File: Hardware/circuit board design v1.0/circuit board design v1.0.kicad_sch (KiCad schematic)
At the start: 0 parts

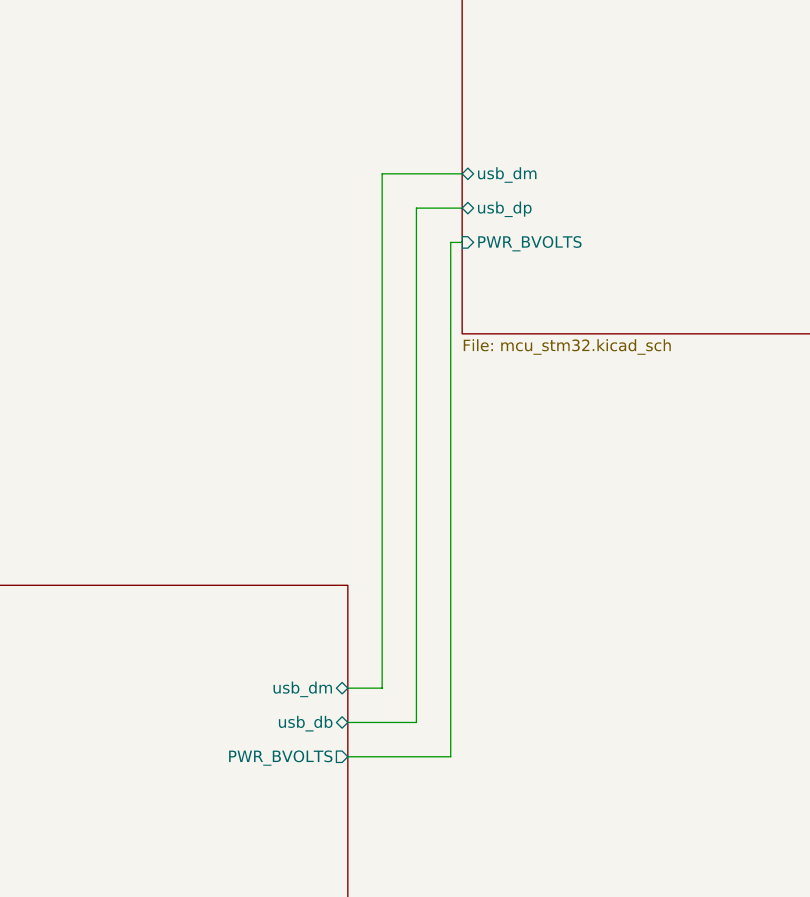
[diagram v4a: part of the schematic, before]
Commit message: Added radio connections to pcb and code
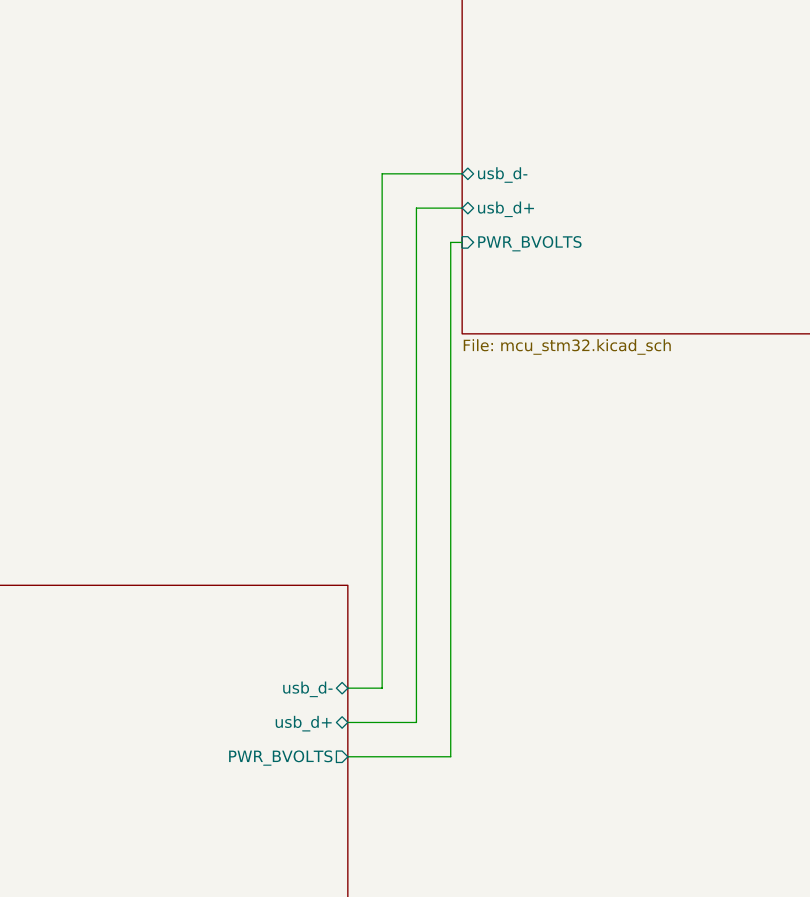
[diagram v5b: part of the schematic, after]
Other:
- sheet MCU ports: added usb_d+, usb_d-; removed usb_dm, usb_dp
- sheet Power ports: added usb_d+, usb_d-; removed usb_db, usb_dm
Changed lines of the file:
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@@
       (effects (font (size 1.27 1.27)) (justify left top))
     )
-    (pin "usb_db" bidirectional (at 78.74 129.54 0)
-      (effects (font (size 1.27 1.27)) (justify right))
-    )
-    (pin "usb_dm" bidirectional (at 78.74 125.73 0)
-      (effects (font (size 1.27 1.27)) (justify right))
-    )
     (pin "PWR_BVOLTS" output (at 78.74 133.35 0)
+      (effects (font (size 1.27 1.27)) (justify right))
+    )
+    (pin "usb_d+" bidirectional (at 78.74 129.54 0)
+      (effects (font (size 1.27 1.27)) (justify right))
+    )
+    (pin "usb_d-" bidirectional (at 78.74 125.73 0)
       (effects (font (size 1.27 1.27)) (justify right))
     )
@@
       (effects (font (size 1.27 1.27)) (justify right))
     )
-    (pin "usb_dp" bidirectional (at 91.44 72.39 180)
+    (pin "UART4_RX" input (at 142.24 67.31 0)
+      (effects (font (size 1.27 1.27)) (justify right))
+    )
+    (pin "UART4_TX" output (at 142.24 71.12 0)
+      (effects (font (size 1.27 1.27)) (justify right))
+    )
+    (pin "PWR_BVOLTS" input (at 91.44 76.2 180)
       (effects (font (size 1.27 1.27)) (justify left))
     )
-    (pin "usb_dm" bidirectional (at 91.44 68.58 180)
+    (pin "usb_d-" bidirectional (at 91.44 68.58 180)
       (effects (font (size 1.27 1.27)) (justify left))
     )
-    (pin "UART4_RX" input (at 142.24 67.31 0)
-      (effects (font (size 1.27 1.27)) (justify right))
-    )
-    (pin "UART4_TX" output (at 142.24 71.12 0)
-      (effects (font (size 1.27 1.27)) (justify right))
-    )
-    (pin "PWR_BVOLTS" input (at 91.44 76.2 180)
+    (pin "usb_d+" bidirectional (at 91.44 72.39 180)
       (effects (font (size 1.27 1.27)) (justify left))
     )
@@
       (reference "#PWR0154") (unit 1) (value "GND") (footprint "")
     )
-    (path "/5a4d8c5a-da32-47cd-8dfd-858fccee0cc7/ef65b748-25fc-45ec-9e41-f3398592a2cf"
+    (path "/0e7a8511-bb07-4cdf-8fc9-61e0cb55f4d9/dcda0964-ba64-44db-bfcf-73cbdcb576fb"
       (reference "#PWR0155") (unit 1) (value "GND") (footprint "")
     )
@@
       (reference "#PWR0158") (unit 1) (value "GND") (footprint "")
     )
+    (path "/0e7a8511-bb07-4cdf-8fc9-61e0cb55f4d9/ad121358-4256-4108-9a2e-f0eebde602b0"
+      (reference "#PWR0159") (unit 1) (value "+3.3VA") (footprint "")
+    )
+    (path "/0e7a8511-bb07-4cdf-8fc9-61e0cb55f4d9/340815ca-5895-42b1-8ca2-152ec3cee0a3"
+      (reference "#PWR0160") (unit 1) (value "+3.3V") (footprint "")
+    )
+    (path "/0e7a8511-bb07-4cdf-8fc9-61e0cb55f4d9/5b47227e-c231-4cc8-894e-420d4391fd7a"
+      (reference "#PWR0161") (unit 1) (value "+3.3V") (footprint "")
+    )
+    (path "/0e7a8511-bb07-4cdf-8fc9-61e0cb55f4d9/88affa64-ff64-412e-9baf-e3fdb3141087"
+      (reference "#PWR0162") (unit 1) (value "GND") (footprint "")
+    )
+    (path "/0e7a8511-bb07-4cdf-8fc9-61e0cb55f4d9/268973f5-9c55-4078-8d40-7eed042f832f"
+      (reference "#PWR0163") (unit 1) (value "GND") (footprint "")
+    )
+    (path "/0e7a8511-bb07-4cdf-8fc9-61e0cb55f4d9/98069769-9eb8-471b-9c87-68beaf30313a"
+      (reference "#PWR0164") (unit 1) (value "GND") (footprint "")
+    )
+    (path "/0e7a8511-bb07-4cdf-8fc9-61e0cb55f4d9/532c95ce-f067-4d69-bc9a-0f63f5e8663b"
+      (reference "#PWR0165") (unit 1) (value "GND") (footprint "")
+    )
+    (path "/b2e7fea0-7ba9-48b0-990f-5c369d704fdf/efda26c1-1b2e-45fc-8118-8714daea6824"
+      (reference "#PWR0166") (unit 1) (value "+3.3V") (footprint "")
+    )
+    (path "/b2e7fea0-7ba9-48b0-990f-5c369d704fdf/6b5ab9a6-ff3f-4ed7-b55a-df06ce82df1b"
+      (reference "#PWR0167") (unit 1) (value "GND") (footprint "")
+    )
     (path "/0e7a8511-bb07-4cdf-8fc9-61e0cb55f4d9/b539404f-fa7b-4ea0-92b0-e63766b84104"
       (reference "C1") (unit 1) (value "100nF") (footprint "Capacitor_SMD:C_0603_1608Metric")
@@
     )
     (path "/5a4d8c5a-da32-47cd-8dfd-858fccee0cc7/51340589-033f-4817-8e4e-cf924c831231"
-      (reference "C16") (unit 1) (value "1uF") (footprint "Capacitor_SMD:C_1206_3216Metric")
+      (reference "C16") (unit 1) (value "4.7uF") (footprint "Capacitor_SMD:C_1206_3216Metric")
     )
     (path "/b2e7fea0-7ba9-48b0-990f-5c369d704fdf/162f214d-2052-405a-a965-466a0e579039"
@@
       (reference "C20") (unit 1) (value "1uF") (footprint "Resistor_SMD:R_0603_1608Metric")
     )
-    (path "/5a4d8c5a-da32-47cd-8dfd-858fccee0cc7/6d36a4e8-6681-4ecb-ac10-10481f840eab"
-      (reference "C21") (unit 1) (value "4.7uF") (footprint "Capacitor_SMD:C_0603_1608Metric")
+    (path "/0e7a8511-bb07-4cdf-8fc9-61e0cb55f4d9/bf57f6fe-2b5b-46fd-a1d6-d64e08f75bfb"
+      (reference "C21") (unit 1) (value "100nF") (footprint "Capacitor_SMD:C_0603_1608Metric")
     )
     (path "/b2e7fea0-7ba9-48b0-990f-5c369d704fdf/0aa13a41-8ef8-47fa-83b9-4f889783ba59"
@@
       (reference "C24") (unit 1) (value "1uF") (footprint "Capacitor_SMD:C_0603_1608Metric_Pad1.08x0.95mm_HandSolder")
     )
+    (path "/0e7a8511-bb07-4cdf-8fc9-61e0cb55f4d9/cf0596e4-7432-4470-9bbd-ca32965dc181"
+      (reference "C25") (unit 1) (value "100nF") (footprint "Capacitor_SMD:C_0603_1608Metric")
+    )
+    (path "/0e7a8511-bb07-4cdf-8fc9-61e0cb55f4d9/77669a4d-e2cb-4a23-aa47-7172f4ddf6f0"
+      (reference "C26") (unit 1) (value "100nF") (footprint "Capacitor_SMD:C_0603_1608Metric")
+    )
     (path "/5a4d8c5a-da32-47cd-8dfd-858fccee0cc7/bba0d31a-418a-4e8f-83f7-a25be8737299"
       (reference "D1") (unit 1) (value "DFLS130L") (footprint "Components:PowerDI123")
@@
       (reference "IC1") (unit 1) (value "BMI088") (footprint "Components:BMI088")
     )
-    (path "/b2e7fea0-7ba9-48b0-990f-5c369d704fdf/e0eee924-6a94-4485-a584-224d836dfad3"
-      (reference "J1") (unit 1) (value "Conn_01x06_Male") (footprint "Connector_PinHeader_2.54mm:PinHeader_2x03_P2.54mm_Vertical")
+    (path "/b2e7fea0-7ba9-48b0-990f-5c369d704fdf/7a7f25b3-bfe0-4615-8ccc-4b6dcd99aa74"
+      (reference "J1") (unit 1) (value "Conn_01x02_Male") (footprint "Connector_PinHeader_2.54mm:PinHeader_1x02_P2.54mm_Vertical")
     )
     (path "/5a4d8c5a-da32-47cd-8dfd-858fccee0cc7/4c1f332c-8bba-42c9-b90b-d64280804d9b"
@@
       (reference "J3") (unit 1) (value "105017-0001") (footprint "MOLEX_105017-0001")
     )
-    (path "/b2e7fea0-7ba9-48b0-990f-5c369d704fdf/71e9a856-f24b-40f9-ad40-3d2bf59b11f7"
-      (reference "J4") (unit 1) (value "Conn_01x04") (footprint "Components:JST_PH_S4B-PH-K_1x04_P2.00mm_Horizontal")
+    (path "/b2e7fea0-7ba9-48b0-990f-5c369d704fdf/a51104d2-c3b8-463e-b304-493dab3c4ff8"
+      (reference "J4") (unit 1) (value "DF13-10P-1.25DS_20_") (footprint "Components:DF1310P125DS20")
+    )
+    (path "/b2e7fea0-7ba9-48b0-990f-5c369d704fdf/3ec3363d-d0bd-4291-ac89-97e625e49bab"
+      (reference "J6") (unit 1) (value "Conn_01x02_Male") (footprint "Connector_PinHeader_2.54mm:PinHeader_1x02_P2.54mm_Vertical")
     )
     (path "/b2e7fea0-7ba9-48b0-990f-5c369d704fdf/8c3483d6-21f9-4d68-878f-71b6b407e760"
@@
       (reference "U8") (unit 1) (value "L80-M39") (footprint "Components:Quectel_L80-R")
     )
+    (path "/0e7a8511-bb07-4cdf-8fc9-61e0cb55f4d9/c8d93d07-b504-4000-86e1-fab3d26059bb"
+      (reference "U9") (unit 1) (value "LIS3MDLTR") (footprint "Components:XDCR_LIS3MDLTR")
+    )
     (path "/b2e7fea0-7ba9-48b0-990f-5c369d704fdf/1523611f-36b3-41d8-aacc-df91fb39802f"
